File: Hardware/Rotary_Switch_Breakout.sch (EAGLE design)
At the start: 8 parts, among them SW1 1x10

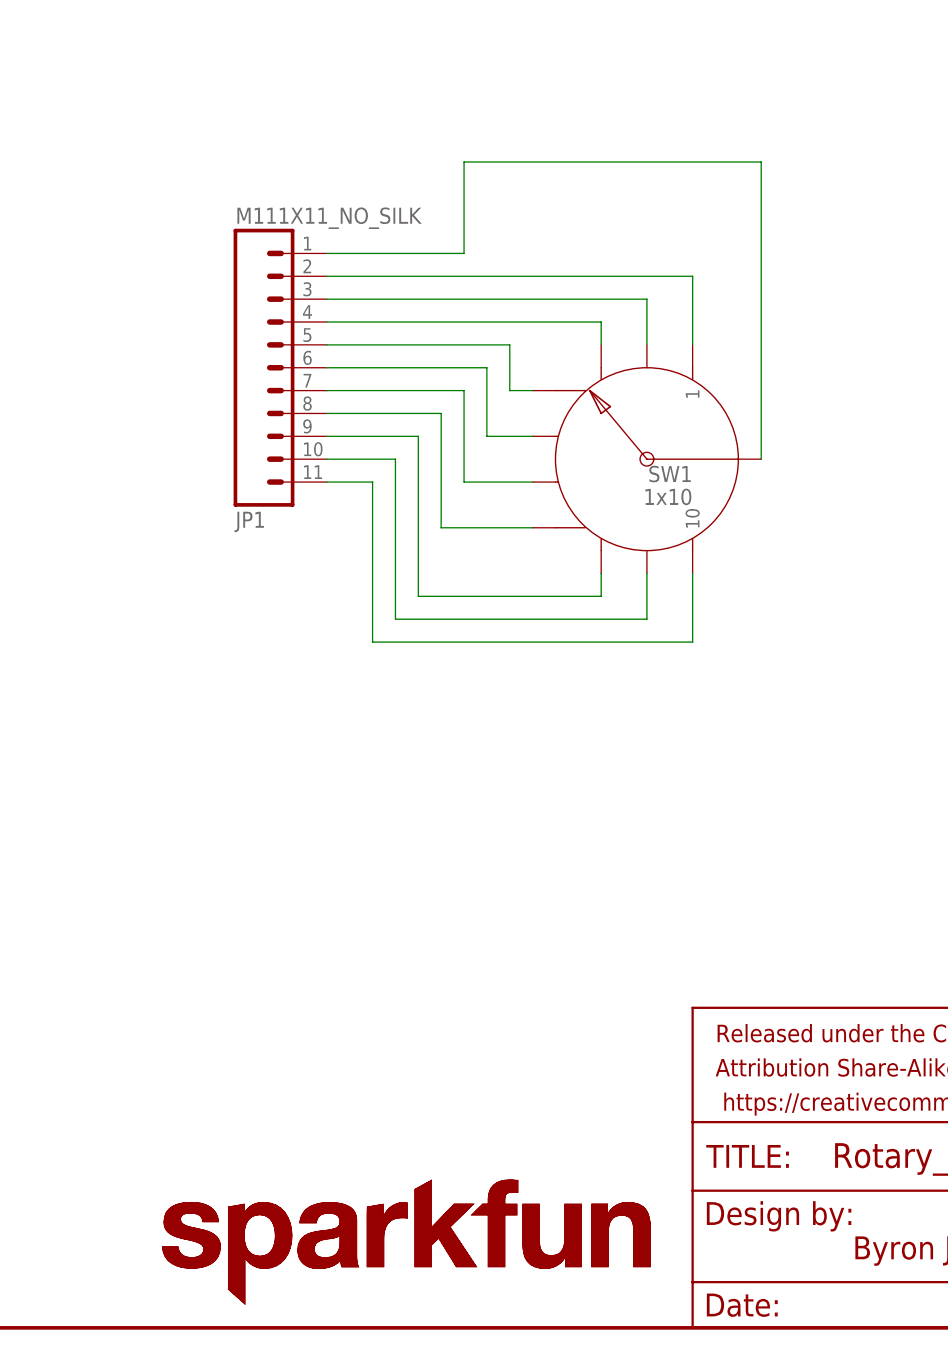
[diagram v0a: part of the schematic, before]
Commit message: Updates to layout
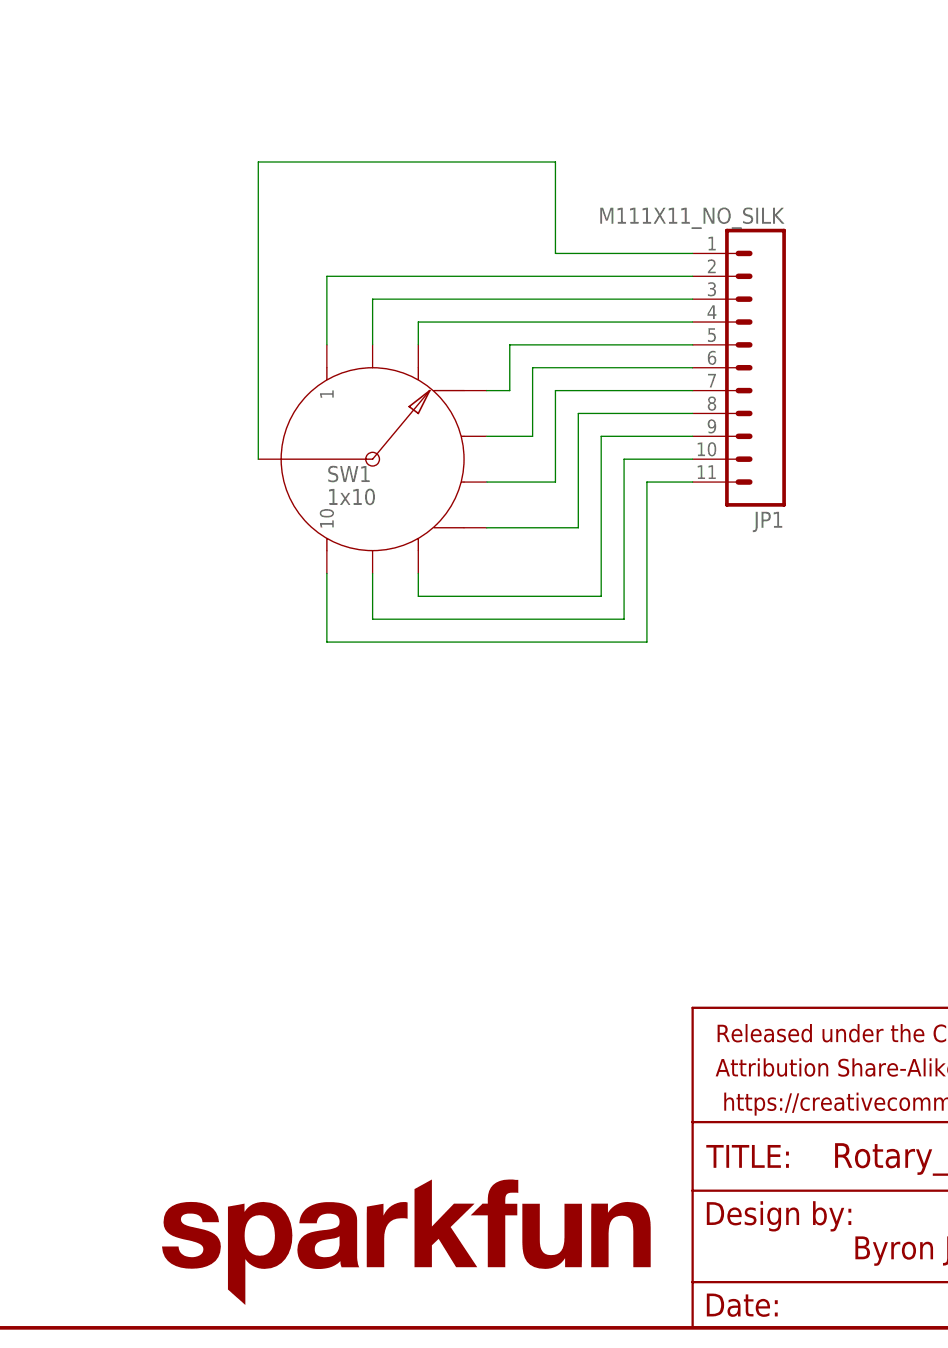
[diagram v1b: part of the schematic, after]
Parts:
- removed LOGO2: SFE_LOGO_NAME.1_INCH, SparkFun-Aesthetics:SFE_LOGO_NAME.1_INCH
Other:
- moved on the sheet: JP1, SW1
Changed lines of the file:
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@@
 <part name="JP1" library="SparkFun-Connectors" deviceset="M11" device="1X11_NO_SILK"/>
 <part name="LOGO1" library="SparkFun-Aesthetics" deviceset="OSHW-LOGO" device="M"/>
-<part name="LOGO2" library="SparkFun-Aesthetics" deviceset="SFE_LOGO_NAME" device=".1_INCH"/>
 <part name="STANDOFF1" library="SparkFun-Electromechanical" deviceset="STAND-OFF" device=""/>
 <part name="STANDOFF2" library="SparkFun-Electromechanical" deviceset="STAND-OFF" device=""/>
@@
 <instance part="FRAME1" gate="G$1" x="0" y="0"/>
 <instance part="FRAME1" gate="G$2" x="147.32" y="0"/>
-<instance part="SW1" gate="G$1" x="142.24" y="96.52" rot="MR0"/>
-<instance part="JP1" gate="G$1" x="96.52" y="106.68" rot="MR180"/>
+<instance part="SW1" gate="G$1" x="111.76" y="96.52"/>
+<instance part="JP1" gate="G$1" x="157.48" y="106.68" rot="R180"/>
 <instance part="LOGO1" gate="G$1" x="236.22" y="27.94"/>
-<instance part="LOGO2" gate="G$1" x="86.36" y="2.54"/>
 <instance part="STANDOFF1" gate="G$1" x="231.14" y="12.7"/>
 <instance part="STANDOFF2" gate="G$1" x="231.14" y="7.62"/>
@@
 <segment>
 <pinref part="JP1" gate="G$1" pin="1"/>
-<wire x1="106.68" y1="119.38" x2="121.92" y2="119.38" width="0.1524" layer="91"/>
-<wire x1="121.92" y1="119.38" x2="121.92" y2="129.54" width="0.1524" layer="91"/>
-<wire x1="121.92" y1="129.54" x2="154.94" y2="129.54" width="0.1524" layer="91"/>
+<wire x1="147.32" y1="119.38" x2="132.08" y2="119.38" width="0.1524" layer="91"/>
+<wire x1="132.08" y1="119.38" x2="132.08" y2="129.54" width="0.1524" layer="91"/>
+<wire x1="132.08" y1="129.54" x2="99.06" y2="129.54" width="0.1524" layer="91"/>
 <pinref part="SW1" gate="G$1" pin="COMMON"/>
-<wire x1="154.94" y1="129.54" x2="154.94" y2="96.52" width="0.1524" layer="91"/>
+<wire x1="99.06" y1="129.54" x2="99.06" y2="96.52" width="0.1524" layer="91"/>
 </segment>
 </net>
@@
 <segment>
 <pinref part="JP1" gate="G$1" pin="2"/>
-<wire x1="106.68" y1="116.84" x2="147.32" y2="116.84" width="0.1524" layer="91"/>
+<wire x1="147.32" y1="116.84" x2="106.68" y2="116.84" width="0.1524" layer="91"/>
 <pinref part="SW1" gate="G$1" pin="1"/>
-<wire x1="147.32" y1="116.84" x2="147.32" y2="109.22" width="0.1524" layer="91"/>
+<wire x1="106.68" y1="116.84" x2="106.68" y2="109.22" width="0.1524" layer="91"/>
 </segment>
 </net>
@@
 <pinref part="SW1" gate="G$1" pin="2"/>
 <pinref part="JP1" gate="G$1" pin="3"/>
-<wire x1="142.24" y1="109.22" x2="142.24" y2="114.3" width="0.1524" layer="91"/>
-<wire x1="142.24" y1="114.3" x2="106.68" y2="114.3" width="0.1524" layer="91"/>
+<wire x1="111.76" y1="109.22" x2="111.76" y2="114.3" width="0.1524" layer="91"/>
+<wire x1="111.76" y1="114.3" x2="147.32" y2="114.3" width="0.1524" layer="91"/>
 </segment>
 </net>
@@
 <segment>
 <pinref part="JP1" gate="G$1" pin="4"/>
-<wire x1="106.68" y1="111.76" x2="137.16" y2="111.76" width="0.1524" layer="91"/>
+<wire x1="147.32" y1="111.76" x2="116.84" y2="111.76" width="0.1524" layer="91"/>
 <pinref part="SW1" gate="G$1" pin="3"/>
-<wire x1="137.16" y1="111.76" x2="137.16" y2="109.22" width="0.1524" layer="91"/>
+<wire x1="116.84" y1="111.76" x2="116.84" y2="109.22" width="0.1524" layer="91"/>
 </segment>
 </net>
@@
 <segment>
 <pinref part="JP1" gate="G$1" pin="5"/>
-<wire x1="106.68" y1="109.22" x2="127" y2="109.22" width="0.1524" layer="91"/>
+<wire x1="147.32" y1="109.22" x2="127" y2="109.22" width="0.1524" layer="91"/>
 <wire x1="127" y1="109.22" x2="127" y2="104.14" width="0.1524" layer="91"/>
 <pinref part="SW1" gate="G$1" pin="4"/>
-<wire x1="127" y1="104.14" x2="129.54" y2="104.14" width="0.1524" layer="91"/>
+<wire x1="127" y1="104.14" x2="124.46" y2="104.14" width="0.1524" layer="91"/>
 </segment>
 </net>
@@
 <segment>
 <pinref part="JP1" gate="G$1" pin="6"/>
-<wire x1="106.68" y1="106.68" x2="124.46" y2="106.68" width="0.1524" layer="91"/>
-<wire x1="124.46" y1="106.68" x2="124.46" y2="99.06" width="0.1524" layer="91"/>
+<wire x1="147.32" y1="106.68" x2="129.54" y2="106.68" width="0.1524" layer="91"/>
+<wire x1="129.54" y1="106.68" x2="129.54" y2="99.06" width="0.1524" layer="91"/>
 <pinref part="SW1" gate="G$1" pin="5"/>
-<wire x1="124.46" y1="99.06" x2="129.54" y2="99.06" width="0.1524" layer="91"/>
+<wire x1="129.54" y1="99.06" x2="124.46" y2="99.06" width="0.1524" layer="91"/>
 </segment>
 </net>
@@
 <segment>
 <pinref part="JP1" gate="G$1" pin="7"/>
-<wire x1="106.68" y1="104.14" x2="121.92" y2="104.14" width="0.1524" layer="91"/>
-<wire x1="121.92" y1="104.14" x2="121.92" y2="93.98" width="0.1524" layer="91"/>
+<wire x1="147.32" y1="104.14" x2="132.08" y2="104.14" width="0.1524" layer="91"/>
+<wire x1="132.08" y1="104.14" x2="132.08" y2="93.98" width="0.1524" layer="91"/>
 <pinref part="SW1" gate="G$1" pin="6"/>
-<wire x1="121.92" y1="93.98" x2="129.54" y2="93.98" width="0.1524" layer="91"/>
+<wire x1="132.08" y1="93.98" x2="124.46" y2="93.98" width="0.1524" layer="91"/>
 </segment>
 </net>
@@
 <segment>
 <pinref part="JP1" gate="G$1" pin="8"/>
-<wire x1="106.68" y1="101.6" x2="119.38" y2="101.6" width="0.1524" layer="91"/>
+<wire x1="147.32" y1="101.6" x2="134.62" y2="101.6" width="0.1524" layer="91"/>
 <pinref part="SW1" gate="G$1" pin="7"/>
-<wire x1="119.38" y1="101.6" x2="119.38" y2="88.9" width="0.1524" layer="91"/>
-<wire x1="119.38" y1="88.9" x2="129.54" y2="88.9" width="0.1524" layer="91"/>
+<wire x1="134.62" y1="101.6" x2="134.62" y2="88.9" width="0.1524" layer="91"/>
+<wire x1="134.62" y1="88.9" x2="124.46" y2="88.9" width="0.1524" layer="91"/>
 </segment>
 </net>
@@
 <segment>
 <pinref part="JP1" gate="G$1" pin="9"/>
-<wire x1="106.68" y1="99.06" x2="116.84" y2="99.06" width="0.1524" layer="91"/>
-<wire x1="116.84" y1="99.06" x2="116.84" y2="81.28" width="0.1524" layer="91"/>
-<wire x1="116.84" y1="81.28" x2="137.16" y2="81.28" width="0.1524" layer="91"/>
+<wire x1="147.32" y1="99.06" x2="137.16" y2="99.06" width="0.1524" layer="91"/>
+<wire x1="137.16" y1="99.06" x2="137.16" y2="81.28" width="0.1524" layer="91"/>
+<wire x1="137.16" y1="81.28" x2="116.84" y2="81.28" width="0.1524" layer="91"/>
 <pinref part="SW1" gate="G$1" pin="8"/>
-<wire x1="137.16" y1="81.28" x2="137.16" y2="83.82" width="0.1524" layer="91"/>
+<wire x1="116.84" y1="81.28" x2="116.84" y2="83.82" width="0.1524" layer="91"/>
 </segment>
 </net>
@@
 <segment>
 <pinref part="SW1" gate="G$1" pin="9"/>
-<wire x1="142.24" y1="83.82" x2="142.24" y2="78.74" width="0.1524" layer="91"/>
-<wire x1="142.24" y1="78.74" x2="114.3" y2="78.74" width="0.1524" layer="91"/>
-<wire x1="114.3" y1="78.74" x2="114.3" y2="96.52" width="0.1524" layer="91"/>
+<wire x1="111.76" y1="83.82" x2="111.76" y2="78.74" width="0.1524" layer="91"/>
+<wire x1="111.76" y1="78.74" x2="139.7" y2="78.74" width="0.1524" layer="91"/>
+<wire x1="139.7" y1="78.74" x2="139.7" y2="96.52" width="0.1524" layer="91"/>
 <pinref part="JP1" gate="G$1" pin="10"/>
-<wire x1="114.3" y1="96.52" x2="106.68" y2="96.52" width="0.1524" layer="91"/>
+<wire x1="139.7" y1="96.52" x2="147.32" y2="96.52" width="0.1524" layer="91"/>
 </segment>
 </net>
@@
 <segment>
 <pinref part="JP1" gate="G$1" pin="11"/>
-<wire x1="106.68" y1="93.98" x2="111.76" y2="93.98" width="0.1524" layer="91"/>
-<wire x1="111.76" y1="93.98" x2="111.76" y2="76.2" width="0.1524" layer="91"/>
-<wire x1="111.76" y1="76.2" x2="147.32" y2="76.2" width="0.1524" layer="91"/>
+<wire x1="147.32" y1="93.98" x2="142.24" y2="93.98" width="0.1524" layer="91"/>
+<wire x1="142.24" y1="93.98" x2="142.24" y2="76.2" width="0.1524" layer="91"/>
+<wire x1="142.24" y1="76.2" x2="106.68" y2="76.2" width="0.1524" layer="91"/>
 <pinref part="SW1" gate="G$1" pin="10"/>
-<wire x1="147.32" y1="76.2" x2="147.32" y2="83.82" width="0.1524" layer="91"/>
+<wire x1="106.68" y1="76.2" x2="106.68" y2="83.82" width="0.1524" layer="91"/>
 </segment>
 </net>

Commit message: Ready to review for reds
Added dimensions, rolled revision # to V10
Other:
- note added: "V10"
- note removed: "V01"
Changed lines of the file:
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@@
 <plain>
 <text x="165.1" y="7.62" size="2.54" layer="94" font="vector">Byron Jacquot</text>
-<text x="238.76" y="7.62" size="2.54" layer="94" font="vector">V01</text>
+<text x="238.76" y="7.62" size="2.54" layer="94" font="vector">V10</text>
 </plain>
 <instances>

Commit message: Revising from review comments.
Now has 4 standoff holes.
Dimensioning is more legible.
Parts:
- renumbered STANDOFF1 to STANDOFF4
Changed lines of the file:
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@@
 <part name="JP1" library="SparkFun-Connectors" deviceset="M11" device="1X11_NO_SILK"/>
 <part name="LOGO1" library="SparkFun-Aesthetics" deviceset="OSHW-LOGO" device="M"/>
-<part name="STANDOFF1" library="SparkFun-Electromechanical" deviceset="STAND-OFF" device=""/>
+<part name="STANDOFF4" library="SparkFun-Electromechanical" deviceset="STAND-OFF" device=""/>
 <part name="STANDOFF2" library="SparkFun-Electromechanical" deviceset="STAND-OFF" device=""/>
 <part name="LOGO3" library="SparkFun-Aesthetics" deviceset="SFE_LOGO_NAME" device=".1_INCH"/>
@@
 <instance part="JP1" gate="G$1" x="157.48" y="106.68" rot="R180"/>
 <instance part="LOGO1" gate="G$1" x="236.22" y="27.94"/>
-<instance part="STANDOFF1" gate="G$1" x="231.14" y="12.7"/>
+<instance part="STANDOFF4" gate="G$1" x="231.14" y="12.7"/>
 <instance part="STANDOFF2" gate="G$1" x="231.14" y="7.62"/>
 <instance part="LOGO3" gate="G$1" x="86.36" y="2.54"/>

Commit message: Updated from QC checklist review.
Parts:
- renumbered SW1 to S1
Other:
- note added: "Taiwan Alpha PN #SR2512F-0110-16F2B-C9-S switch contacts are rated to maximum of 300 mA, 125 VAC."
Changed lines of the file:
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@@
 <parts>
 <part name="FRAME1" library="SparkFun-Aesthetics" deviceset="FRAME-LETTER" device=""/>
-<part name="SW1" library="SparkFun-Electromechanical" deviceset="SWITCH_ROTARY_1X10" device="KIT" value="1x10"/>
+<part name="S1" library="SparkFun-Electromechanical" deviceset="SWITCH_ROTARY_1X10" device="KIT" value="1x10"/>
 <part name="JP1" library="SparkFun-Connectors" deviceset="M11" device="1X11_NO_SILK"/>
 <part name="LOGO1" library="SparkFun-Aesthetics" deviceset="OSHW-LOGO" device="M"/>
@@
 <text x="165.1" y="7.62" size="2.54" layer="94" font="vector">Byron Jacquot</text>
 <text x="238.76" y="7.62" size="2.54" layer="94" font="vector">V10</text>
+<text x="149.86" y="38.1" size="2.54" layer="94">Taiwan Alpha PN #SR2512F-0110-16F2B-C9-S
+ switch contacts are rated to maximum of
+300 mA, 125 VAC.</text>
 </plain>
 <instances>
 <instance part="FRAME1" gate="G$1" x="0" y="0"/>
 <instance part="FRAME1" gate="G$2" x="147.32" y="0"/>
-<instance part="SW1" gate="G$1" x="111.76" y="96.52"/>
+<instance part="S1" gate="G$1" x="111.76" y="96.52"/>
 <instance part="JP1" gate="G$1" x="157.48" y="106.68" rot="R180"/>
 <instance part="LOGO1" gate="G$1" x="236.22" y="27.94"/>
@@
 <wire x1="147.32" y1="119.38" x2="132.08" y2="119.38" width="0.1524" layer="91"/>
 <wire x1="132.08" y1="119.38" x2="132.08" y2="129.54" width="0.1524" layer="91"/>
-<wire x1="132.08" y1="129.54" x2="99.06" y2="129.54" width="0.1524" layer="91"/>
-<pinref part="SW1" gate="G$1" pin="COMMON"/>
-<wire x1="99.06" y1="129.54" x2="99.06" y2="96.52" width="0.1524" layer="91"/>
+<wire x1="132.08" y1="129.54" x2="96.52" y2="129.54" width="0.1524" layer="91"/>
+<pinref part="S1" gate="G$1" pin="COMMON"/>
+<wire x1="96.52" y1="129.54" x2="96.52" y2="96.52" width="0.1524" layer="91"/>
+<wire x1="96.52" y1="96.52" x2="99.06" y2="96.52" width="0.1524" layer="91"/>
 </segment>
 </net>
@@
 <pinref part="JP1" gate="G$1" pin="2"/>
 <wire x1="147.32" y1="116.84" x2="106.68" y2="116.84" width="0.1524" layer="91"/>
-<pinref part="SW1" gate="G$1" pin="1"/>
+<pinref part="S1" gate="G$1" pin="1"/>
 <wire x1="106.68" y1="116.84" x2="106.68" y2="109.22" width="0.1524" layer="91"/>
 </segment>
@@
 <net name="N$3" class="0">
 <segment>
-<pinref part="SW1" gate="G$1" pin="2"/>
+<pinref part="S1" gate="G$1" pin="2"/>
 <pinref part="JP1" gate="G$1" pin="3"/>
 <wire x1="111.76" y1="109.22" x2="111.76" y2="114.3" width="0.1524" layer="91"/>
@@
 <pinref part="JP1" gate="G$1" pin="4"/>
 <wire x1="147.32" y1="111.76" x2="116.84" y2="111.76" width="0.1524" layer="91"/>
-<pinref part="SW1" gate="G$1" pin="3"/>
+<pinref part="S1" gate="G$1" pin="3"/>
 <wire x1="116.84" y1="111.76" x2="116.84" y2="109.22" width="0.1524" layer="91"/>
 </segment>
@@
 <wire x1="147.32" y1="109.22" x2="127" y2="109.22" width="0.1524" layer="91"/>
 <wire x1="127" y1="109.22" x2="127" y2="104.14" width="0.1524" layer="91"/>
-<pinref part="SW1" gate="G$1" pin="4"/>
+<pinref part="S1" gate="G$1" pin="4"/>
 <wire x1="127" y1="104.14" x2="124.46" y2="104.14" width="0.1524" layer="91"/>
 </segment>
@@
 <wire x1="147.32" y1="106.68" x2="129.54" y2="106.68" width="0.1524" layer="91"/>
 <wire x1="129.54" y1="106.68" x2="129.54" y2="99.06" width="0.1524" layer="91"/>
-<pinref part="SW1" gate="G$1" pin="5"/>
+<pinref part="S1" gate="G$1" pin="5"/>
 <wire x1="129.54" y1="99.06" x2="124.46" y2="99.06" width="0.1524" layer="91"/>
 </segment>
@@
 <wire x1="147.32" y1="104.14" x2="132.08" y2="104.14" width="0.1524" layer="91"/>
 <wire x1="132.08" y1="104.14" x2="132.08" y2="93.98" width="0.1524" layer="91"/>
-<pinref part="SW1" gate="G$1" pin="6"/>
+<pinref part="S1" gate="G$1" pin="6"/>
 <wire x1="132.08" y1="93.98" x2="124.46" y2="93.98" width="0.1524" layer="91"/>
 </segment>
@@
 <pinref part="JP1" gate="G$1" pin="8"/>
 <wire x1="147.32" y1="101.6" x2="134.62" y2="101.6" width="0.1524" layer="91"/>
-<pinref part="SW1" gate="G$1" pin="7"/>
+<pinref part="S1" gate="G$1" pin="7"/>
 <wire x1="134.62" y1="101.6" x2="134.62" y2="88.9" width="0.1524" layer="91"/>
 <wire x1="134.62" y1="88.9" x2="124.46" y2="88.9" width="0.1524" layer="91"/>
@@
 <wire x1="137.16" y1="99.06" x2="137.16" y2="81.28" width="0.1524" layer="91"/>
 <wire x1="137.16" y1="81.28" x2="116.84" y2="81.28" width="0.1524" layer="91"/>
-<pinref part="SW1" gate="G$1" pin="8"/>
+<pinref part="S1" gate="G$1" pin="8"/>
 <wire x1="116.84" y1="81.28" x2="116.84" y2="83.82" width="0.1524" layer="91"/>
 </segment>
@@
 <net name="N$10" class="0">
 <segment>
-<pinref part="SW1" gate="G$1" pin="9"/>
+<pinref part="S1" gate="G$1" pin="9"/>
 <wire x1="111.76" y1="83.82" x2="111.76" y2="78.74" width="0.1524" layer="91"/>
 <wire x1="111.76" y1="78.74" x2="139.7" y2="78.74" width="0.1524" layer="91"/>
@@
 <wire x1="142.24" y1="93.98" x2="142.24" y2="76.2" width="0.1524" layer="91"/>
 <wire x1="142.24" y1="76.2" x2="106.68" y2="76.2" width="0.1524" layer="91"/>
-<pinref part="SW1" gate="G$1" pin="10"/>
+<pinref part="S1" gate="G$1" pin="10"/>
 <wire x1="106.68" y1="76.2" x2="106.68" y2="83.82" width="0.1524" layer="91"/>
 </segment>
@@
 </schematic>
 </drawing>
+<compatibility>
+<note version="6.3" minversion="6.2.2" severity="warning">
+Since Version 6.2.2 text objects can contain more than one line,
+which will not be processed correctly with this version.
+</note>
+</compatibility>
 </eagle>
